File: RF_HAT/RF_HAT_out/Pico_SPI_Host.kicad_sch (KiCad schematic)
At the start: 3 parts, among them U3 RaspberryPi_Pico

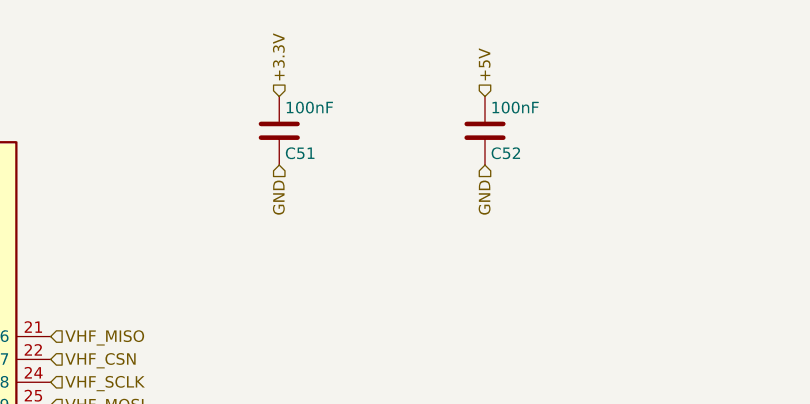
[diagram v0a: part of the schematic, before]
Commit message: switch to SMD pico
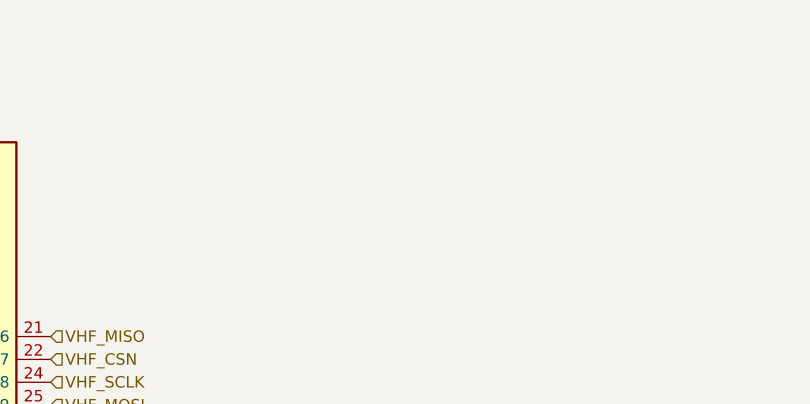
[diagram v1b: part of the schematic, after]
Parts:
- removed C51, C52: 100nF, Capacitor_SMD:C_0402_1005Metric, symbol Device:C
- U3: footprint Module:RaspberryPi_Pico_Common_Unspecified -> Module:RaspberryPi_Pico_Common_SMD

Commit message: switched to 0603 for all passives
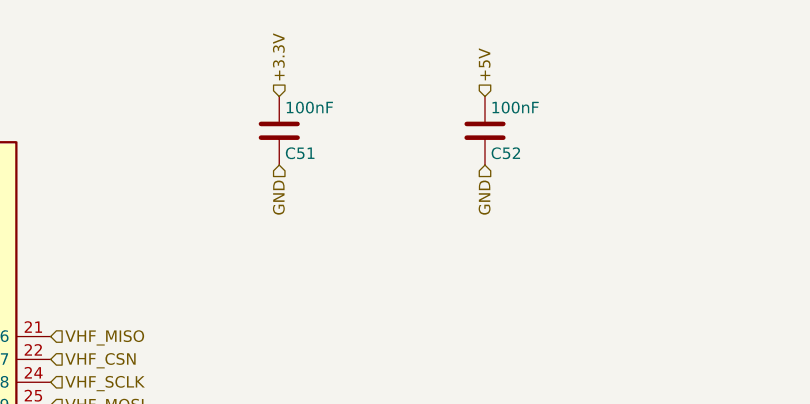
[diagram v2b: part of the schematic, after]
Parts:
- added C51, C52: 100nF, Capacitor_SMD:C_0603_1608Metric, symbol Device:C
- U3: footprint Module:RaspberryPi_Pico_Common_SMD -> Module:RaspberryPi_Pico_SMD; hierarchy_path /03cc9bb1-75ec-4755-9977-259c49401791/9ee7e274-140e-48fc-a7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 -> /bd07fb41-9ea7-4d0f-b403-cbcdc979b1cd/16f3d7a1-68b1-4f0c-96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; root_uuid 03cc9bb1-75ec-4755-9977-259c49401791 -> bd07fb41-9ea7-4d0f-b403-cbcdc979b1cd
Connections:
- net +3.3V: now also C51.1
- net +5V: now also C52.1
- net GND: now also C51.2, C52.2

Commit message: first routing of signals
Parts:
- removed C51, C52: 100nF, Capacitor_SMD:C_0603_1608Metric, symbol Device:C
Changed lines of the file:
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@@
 	(hierarchical_label "+3.3V"
 		(shape input)
-		(at 99.06 29.21 90)
-		(effects
-			(font
-				(size 1.27 1.27)
-			)
-			(justify left)
-		)
-	)
-	(hierarchical_label "+3.3V"
-		(shape input)
 		(at 55.88 30.48 90)
 		(effects
@@
 		)
 	)
-	(hierarchical_label "GND"
-		(shape input)
-		(at 99.06 36.83 270)
-		(effects
-			(font
-				(size 1.27 1.27)
-			)
-			(justify right)
-		)
-	)
 	(hierarchical_label "VHF_MOSI"
 		(shape input)
@@
 		)
 	)
-	(hierarchical_label "GND"
-		(shape input)
-		(at 121.92 36.83 270)
-		(effects
-			(font
-				(size 1.27 1.27)
-			)
-			(justify right)
-		)
-	)
 	(hierarchical_label "VHF_MISO"
 		(shape input)
@@
 			)
 			(justify right)
-		)
-	)
-	(hierarchical_label "+5V"
-		(shape input)
-		(at 121.92 29.21 90)
-		(effects
-			(font
-				(size 1.27 1.27)
-			)
-			(justify left)
 		)
 	)
@@
 					(unit 1)
 				)
-			)
-		)
-	)
-	(symbol
-		(lib_id "Device:C")
-		(at 99.06 33.02 0)
-		(unit 1)
-		(exclude_from_sim no)
-		(in_bom yes)
-		(on_board yes)
-		(dnp no)
-		(property "Reference" "C51"
-			(at 99.695 35.56 0)
-			(effects
-				(font
-					(size 1.27 1.27)
-				)
-				(justify left)
-			)
-		)
-		(property "Value" "100nF"
-			(at 99.695 30.48 0)
-			(effects
-				(font
-					(size 1.27 1.27)
-				)
-				(justify left)
-			)
-		)
-		(property "Footprint" "Capacitor_SMD:C_0603_1608Metric"
-			(at 100.0252 29.21 0)
-			(effects
-				(font
-					(size 1.27 1.27)
-				)
-				(hide yes)
-			)
-		)
-		(property "Datasheet" ""
-			(at 99.06 33.02 0)
-			(effects
-				(font
-					(size 1.27 1.27)
-				)
-			)
-		)
-		(property "Description" ""
-			(at 99.06 33.02 0)
-			(effects
-				(font
-					(size 1.27 1.27)
-				)
-			)
-		)
-		(property "hierarchy_path" "/bd07fb41-9ea7-4d0f-b403-cbcdc979b1cd/16f3d7a1-68b1-4f0c-967e-8cb2238fdf39"
-			(at 101.6 38.0999 0)
-			(effects
-				(font
-					(size 1.27 1.27)
-				)
-				(hide yes)
-			)
-		)
-		(property "project_name" "RF_HAT"
-			(at 101.6 38.0999 0)
-			(effects
-				(font
-					(size 1.27 1.27)
-				)
-				(hide yes)
-			)
-		)
-		(property "root_uuid" "bd07fb41-9ea7-4d0f-b403-cbcdc979b1cd"
-			(at 101.6 38.0999 0)
-			(effects
-				(font
-					(size 1.27 1.27)
-				)
-				(hide yes)
-			)
-		)
-		(pin "1"
-		)
-		(pin "2"
-		)
-		(instances
-			(project ""
-				(path "/bd07fb41-9ea7-4d0f-b403-cbcdc979b1cd/16f3d7a1-68b1-4f0c-967e-8cb2238fdf39"
-					(reference "C51")
-					(unit 1)
-				)
-			)
-		)
-	)
-	(symbol
-		(lib_id "Device:C")
-		(at 121.92 33.02 0)
-		(unit 1)
-		(exclude_from_sim no)
-		(in_bom yes)
-		(on_board yes)
-		(dnp no)
-		(property "Reference" "C52"
-			(at 122.555 35.56 0)
-			(effects
-				(font
-					(size 1.27 1.27)
-				)
-				(justify left)
-			)
-		)
-		(property "Value" "100nF"
-			(at 122.555 30.48 0)
-			(effects
-				(font
-					(size 1.27 1.27)
-				)
-				(justify left)
-			)
-		)
-		(property "Footprint" "Capacitor_SMD:C_0603_1608Metric"
-			(at 122.8852 29.21 0)
-			(effects
-				(font
-					(size 1.27 1.27)
-				)
-				(hide yes)
-			)
-		)
-		(property "Datasheet" ""
-			(at 121.92 33.02 0)
-			(effects
-				(font
-					(size 1.27 1.27)
-				)
-			)
-		)
-		(property "Description" ""
-			(at 121.92 33.02 0)
-			(effects
-				(font
-					(size 1.27 1.27)
-				)
-			)
-		)
-		(property "hierarchy_path" "/bd07fb41-9ea7-4d0f-b403-cbcdc979b1cd/16f3d7a1-68b1-4f0c-967e-8cb2238fdf39"
-			(at 124.46 38.0999 0)
-			(effects
-				(font
-					(size 1.27 1.27)
-				)
-				(hide yes)
-			)
-		)
-		(property "project_name" "RF_HAT"
-			(at 124.46 38.0999 0)
-			(effects
-				(font
-					(size 1.27 1.27)
-				)
-				(hide yes)
-			)
-		)
-		(property "root_uuid" "bd07fb41-9ea7-4d0f-b403-cbcdc979b1cd"
-			(at 124.46 38.0999 0)
-			(effects
-				(font
-					(size 1.27 1.27)
-				)
-				(hide yes)
-			)
-		)
-		(pin "1"
-		)
-		(pin "2"
-		)
-		(instances
-			(project ""
-				(path "/bd07fb41-9ea7-4d0f-b403-cbcdc979b1cd/16f3d7a1-68b1-4f0c-967e-8cb2238fdf39"
-					(reference "C52")
-					(unit 1)
-				)

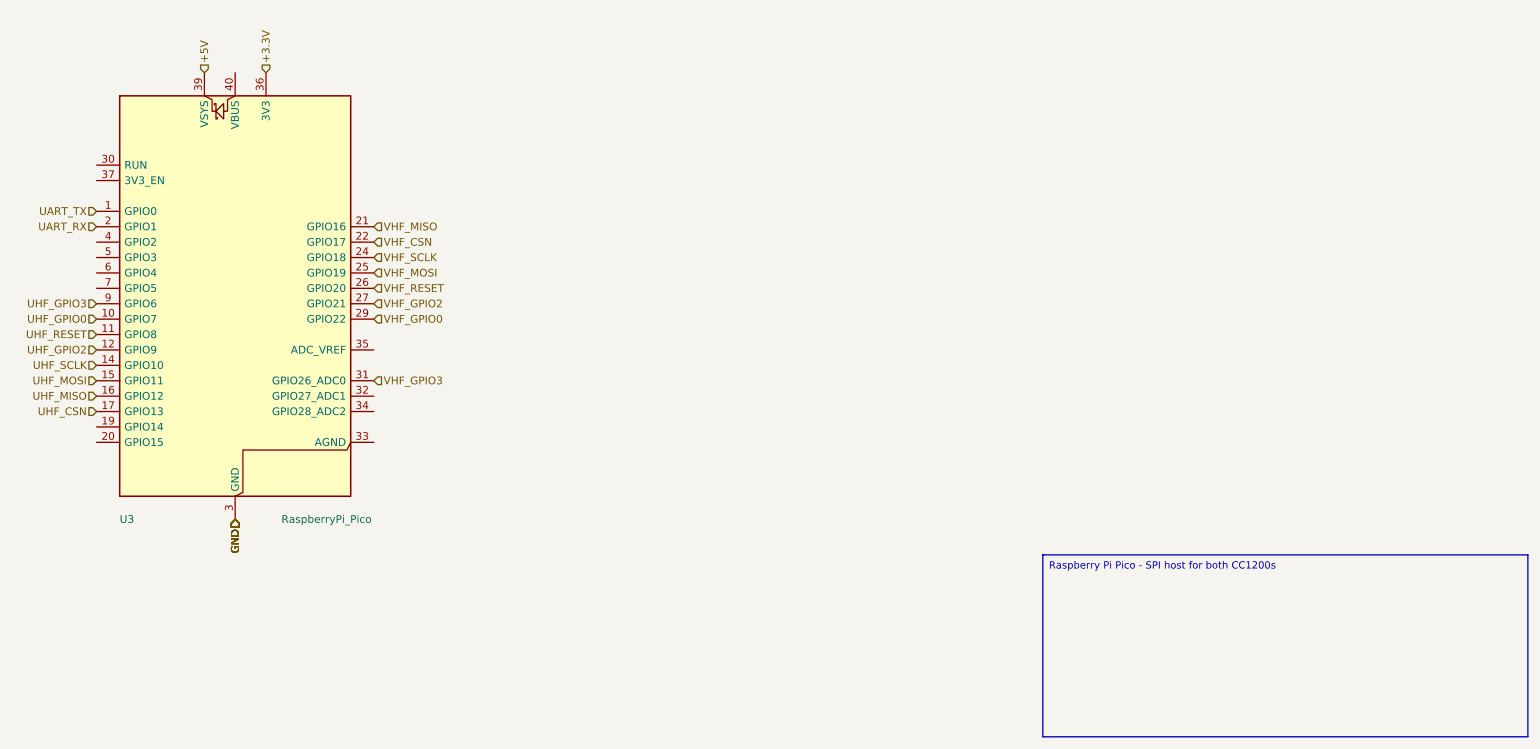
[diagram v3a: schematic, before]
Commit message: Restructured kicad schematic for CC1200 PI_HAT readablitity based on M17 reference schematics
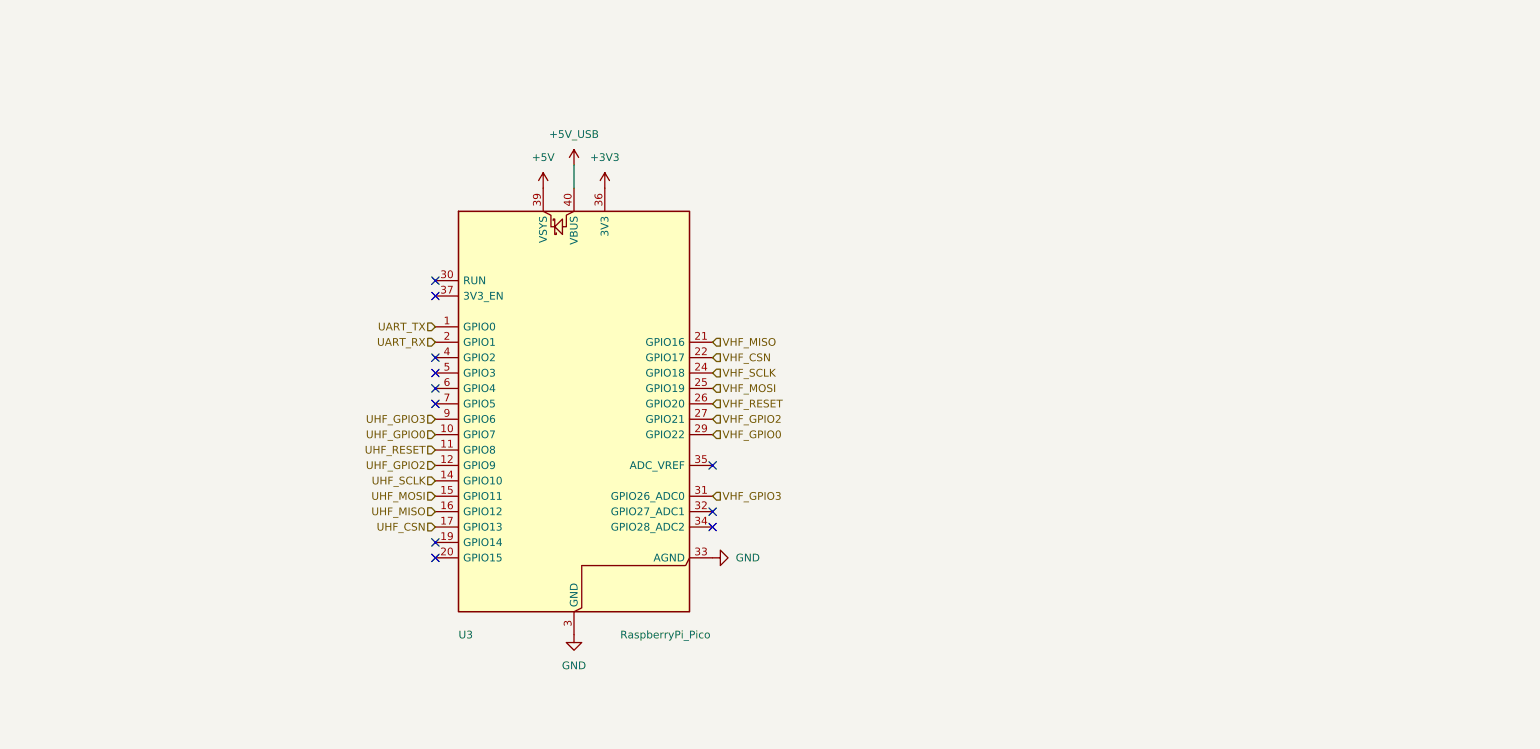
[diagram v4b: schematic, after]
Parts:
- U3: footprint Module:RaspberryPi_Pico_SMD -> Module:RaspberryPi_Pico_Common_Unspecified; hierarchy_path /bd07fb41-9ea7-4d0f-b403-cbcdc979b1cd/16f3d7a1-68b1-4f0c-96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 -> /300cf3d4-e317-44c8-acd8-5f9989779c7c/3e644d4e-3c70-4dba-b4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; root_uuid bd07fb41-9ea7-4d0f-b403-cbcdc979b1cd -> 300cf3d4-e317-44c8-acd8-5f9989779c7c
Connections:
- net GND: now also U3.33 (AGND)
- net +5V_USB: now reaches U3.40 (VBUS)
- net +3.3V renamed +3V3
- no-connect marks 0 -> 11

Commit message: added board edge and connector placement
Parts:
- U3: footprint Module:RaspberryPi_Pico_Common_Unspecified -> Module:RaspberryPi_Pico_SMD
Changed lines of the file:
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@@
 			)
 		)
-		(property "Footprint" "Module:RaspberryPi_Pico_Common_Unspecified"
+		(property "Footprint" "Module:RaspberryPi_Pico_SMD"
 			(at 106.68 40.64 0)
 			(effects

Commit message: did final routing and added Farnell and LCSC numbers to all components
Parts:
- U3: Farnell (none) -> 3643332
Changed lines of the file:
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@@
+			)
+		)
+		(property "Farnell" "3643332"
+			(at 106.68 87.63 0)
+			(effects
+				(font
+					(size 1.27 1.27)
+				)
+				(hide yes)
 			)
 		)

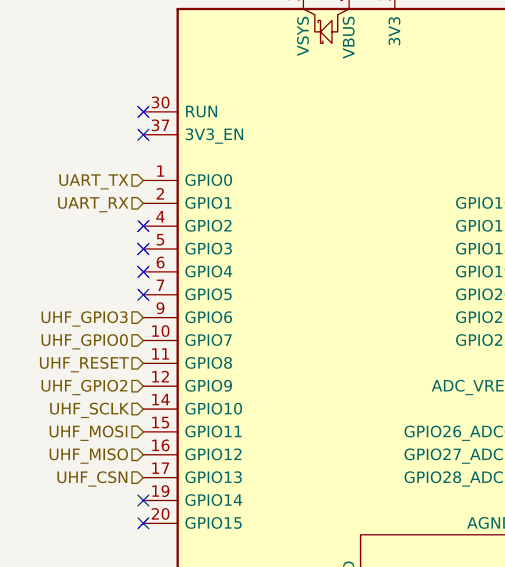
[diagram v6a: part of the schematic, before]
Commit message: update RF_HAT to have WS2812 and buzzer. Start on webserver interface with demo visuals, integration in satnogs system, dual SPI and UART to USB on the Pi_HAT, update readme's
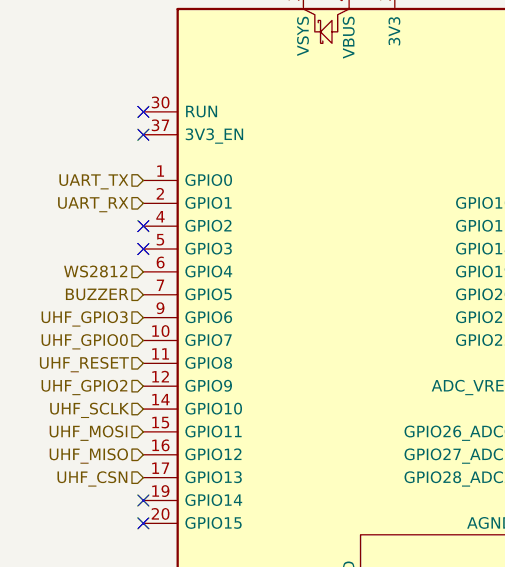
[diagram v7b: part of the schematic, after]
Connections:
- net WS2812: now reaches U3.6 (GPIO4)
- net BUZZER: now reaches U3.7 (GPIO5)
- no-connect marks 11 -> 9
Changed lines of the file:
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@@
+	)
+	(no_connect
+		(at 83.82 77.47)
 	)
 	(no_connect
@@
 	)
 	(no_connect
-		(at 83.82 82.55)
+		(at 83.82 64.77)
+	)
+	(no_connect
+		(at 129.54 105.41)
+	)
+	(no_connect
+		(at 83.82 107.95)
+	)
+	(no_connect
+		(at 83.82 67.31)
 	)
 	(no_connect
 		(at 83.82 80.01)
-	)
-	(no_connect
-		(at 83.82 64.77)
-	)
-	(no_connect
-		(at 83.82 85.09)
-	)
-	(no_connect
-		(at 83.82 77.47)
-	)
-	(no_connect
-		(at 129.54 105.41)
-	)
-	(no_connect
-		(at 83.82 107.95)
-	)
-	(no_connect
-		(at 83.82 67.31)
 	)
 	(wire
@@
 		)
 	)
+	(hierarchical_label "WS2812"
+		(shape input)
+		(at 83.82 82.55 180)
+		(effects
+			(font
+				(size 1.27 1.27)
+			)
+			(justify right)
+		)
+	)
+	(hierarchical_label "BUZZER"
+		(shape input)
+		(at 83.82 85.09 180)
+		(effects
+			(font
+				(size 1.27 1.27)
+			)
+			(justify right)
+		)
+	)
